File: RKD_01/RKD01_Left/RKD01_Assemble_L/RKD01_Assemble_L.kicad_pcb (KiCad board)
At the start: 2 copper layers, 209.6 x 126.2 mm, 86 parts, among them J1 TRRS, M1 Mark, M2 Mark, M3 Mark, M4 Mark, M5 Mark, M6 Mark, SW1 SW_Push, SW10 SW_Push, SW11 SW_Push, SW12 SW_Push, SW13 SW_Push, SW14 SW_Push, SW15 SW_Push, SW16 SW_Push, SW17 SW_Push, SW18 SW_Push, SW19 SW_Push, SW2 SW_Push, SW20 SW_Push, SW21 SW_Push, SW22 SW_Push, SW23 SW_Push, SW24 SW_Push, SW25 SW_Push, SW26 SW_Push, SW27 SW_Push, SW28 SW_Push, SW29 SW_Push, SW3 SW_Push, SW30 SW_Push, SW31 SW_Push, SW32 SW_Push, SW33 SW_Push, SW34 SW_Push, SW35 SW_Push, SW36 SW_Push, SW37 SW_Push, SW38 SW_Push, SW39 SW_Push, SW4 SW_Push, SW5 SW_Push, SW6 SW_Push, SW7 SW_Push, SW8 SW_Push, SW9 SW_Push, U1 ProMicro

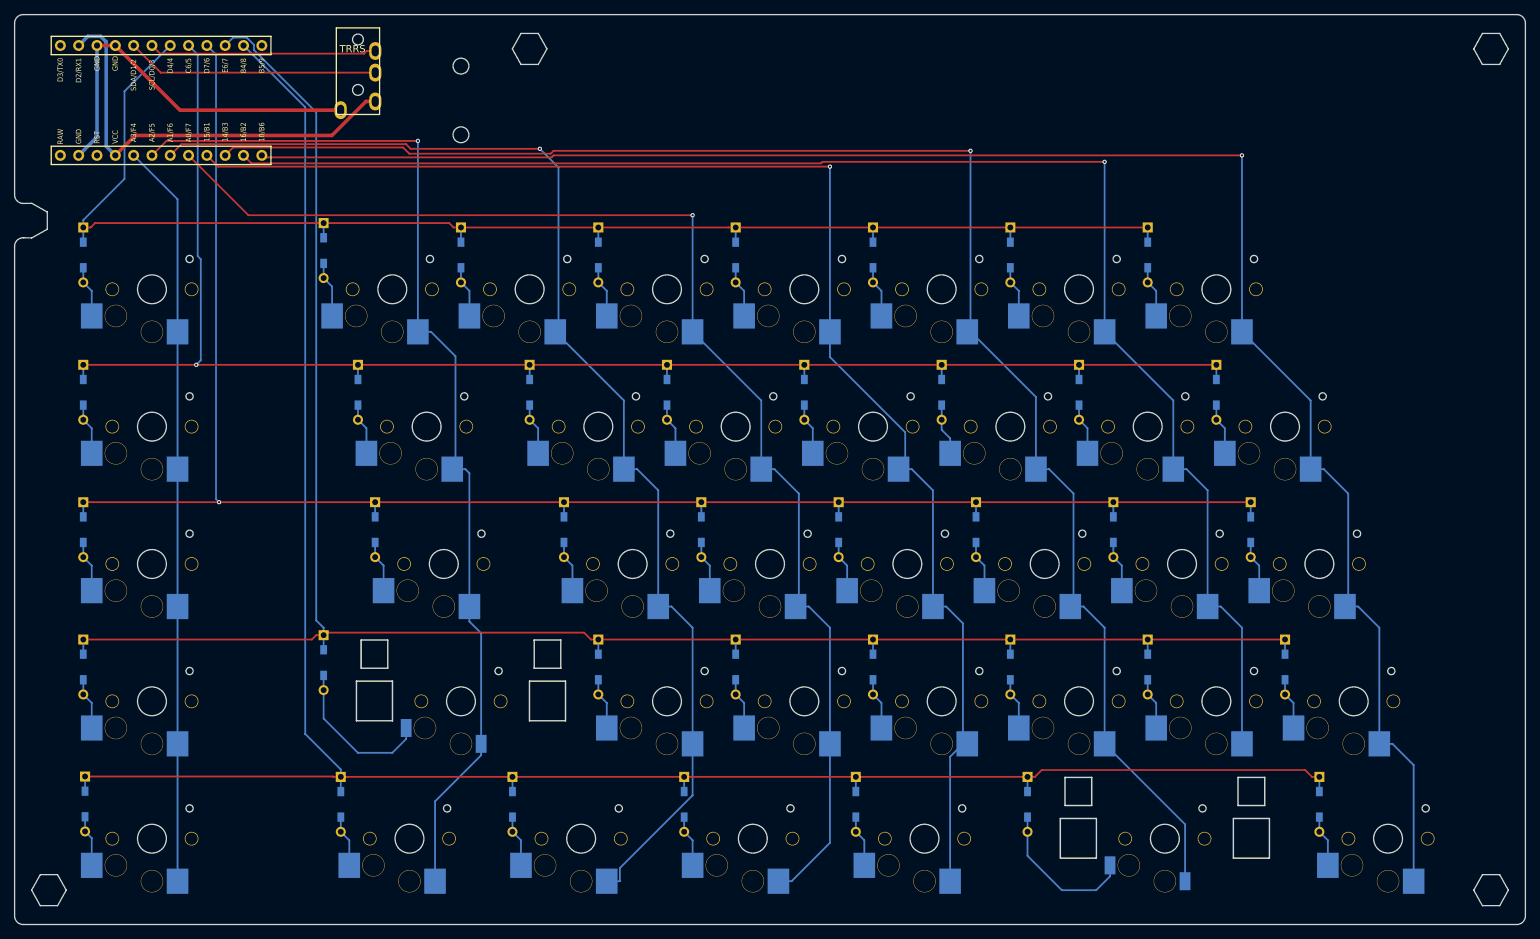
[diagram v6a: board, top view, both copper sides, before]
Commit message: ダイオードが微妙にずれていたので修正
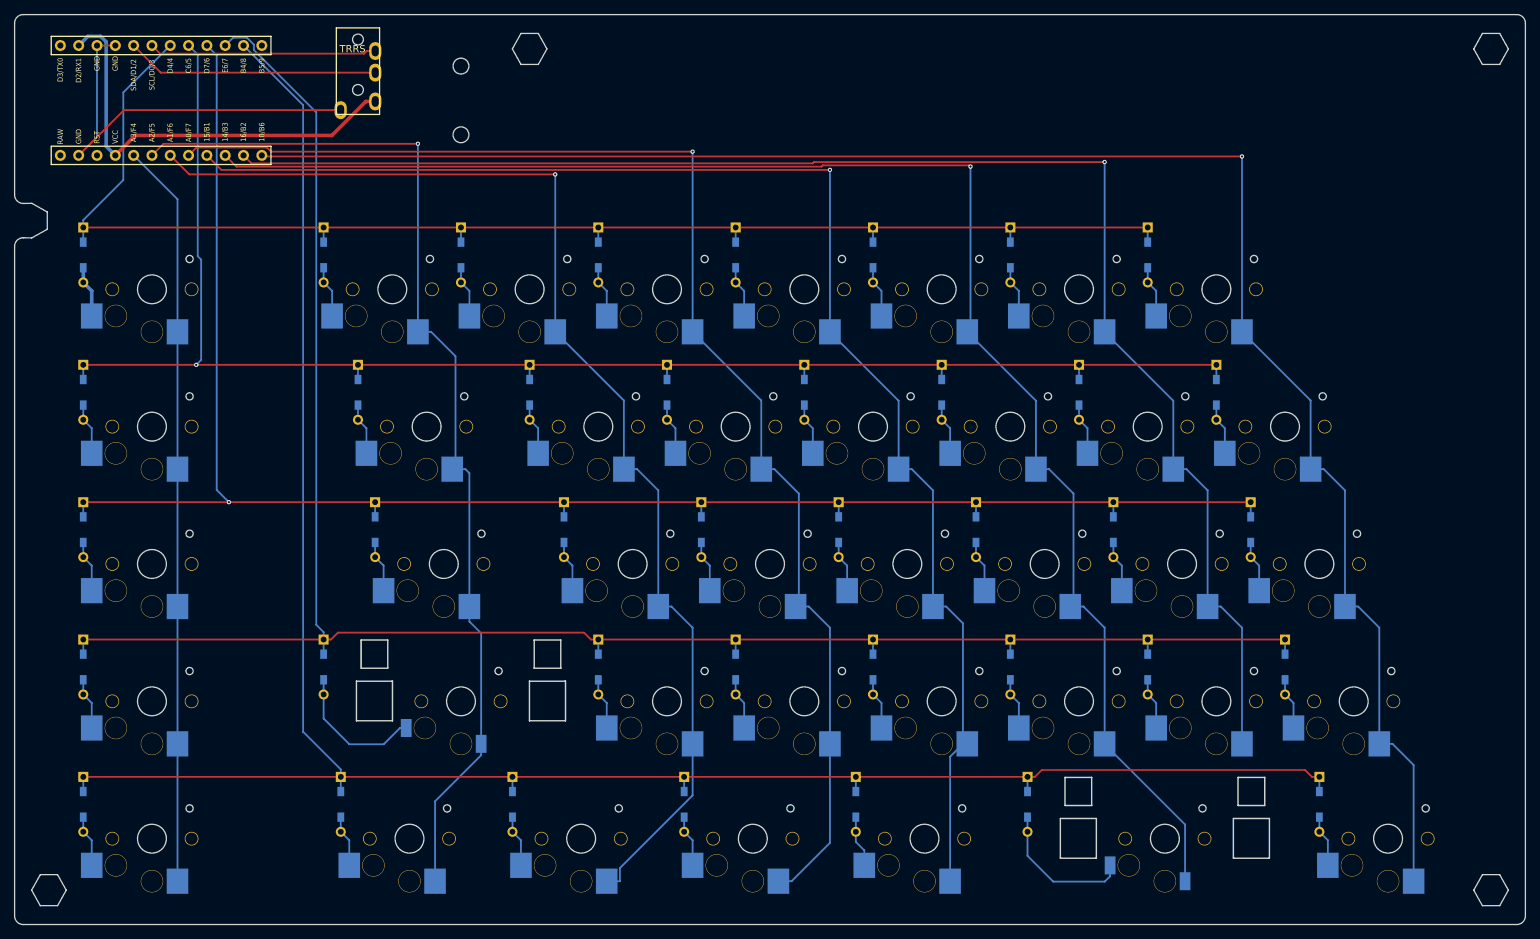
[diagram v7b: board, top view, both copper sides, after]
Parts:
- moved D6 0.61 mm to (64.3, 52.4)
- moved D9 0.61 mm to (64.3, 109.5)
- moved D5 0.25 mm to (31.0, 128.6)
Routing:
- net Col3: track 180.0 -> 186.0 mm
- net GND: track 53.8 -> 57.8 mm
- net Col2: track 171.3 -> 168.6 mm
- net Net-(D9-A): track 21.7 -> 19.2 mm
- net Col5: track 220.8 -> 218.6 mm
- net Net-(D30-A): track 21.1 -> 20.1 mm
- net Col4: track 197.7 -> 197.0 mm
- net Row3: track 274.5 -> 275.1 mm
- net Net-(D6-A): track 7.78 -> 7.17 mm
- net Row2: track 242.2 -> 242.8 mm
- net Col1: track 149.0 -> 148.4 mm
- net Row0: track 194.7 -> 194.2 mm

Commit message: v1.5
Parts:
- added M7: Mark, kbd_Hole:m2_Spacer_Hole_hex, F.Cu at (178.6, 66.7)
- added M8: Mark, kbd_Hole:m2_Spacer_Hole_hex, F.Cu at (90.5, 104.8)
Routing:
- net GND: track 57.8 -> 53.8 mm
- net Row3: track 275.1 -> 279.1 mm
- net Col6: track 210.7 -> 213.5 mm
- net Col5: track 218.6 -> 221.1 mm
- net Row1: track 218.7 -> 220.9 mm
- net Net-(D9-A): track 19.2 -> 21.1 mm
- net Col3: track 186.0 -> 187.4 mm
- net Col2: track 168.6 -> 169.9 mm
- net Col4: track 197.0 -> 198.1 mm
- net Net-(D30-A): track 20.1 -> 21.1 mm
- net Col7: track 249.6 -> 250.3 mm
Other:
- board text added: "RKD01_Left v1.5"
- board text removed: "RKD01_Left v1.0"
